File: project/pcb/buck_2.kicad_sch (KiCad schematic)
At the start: 15 parts, among them U1 IR2110PBF DIP14, U2 L7805CV, U3 SN74HCT14N

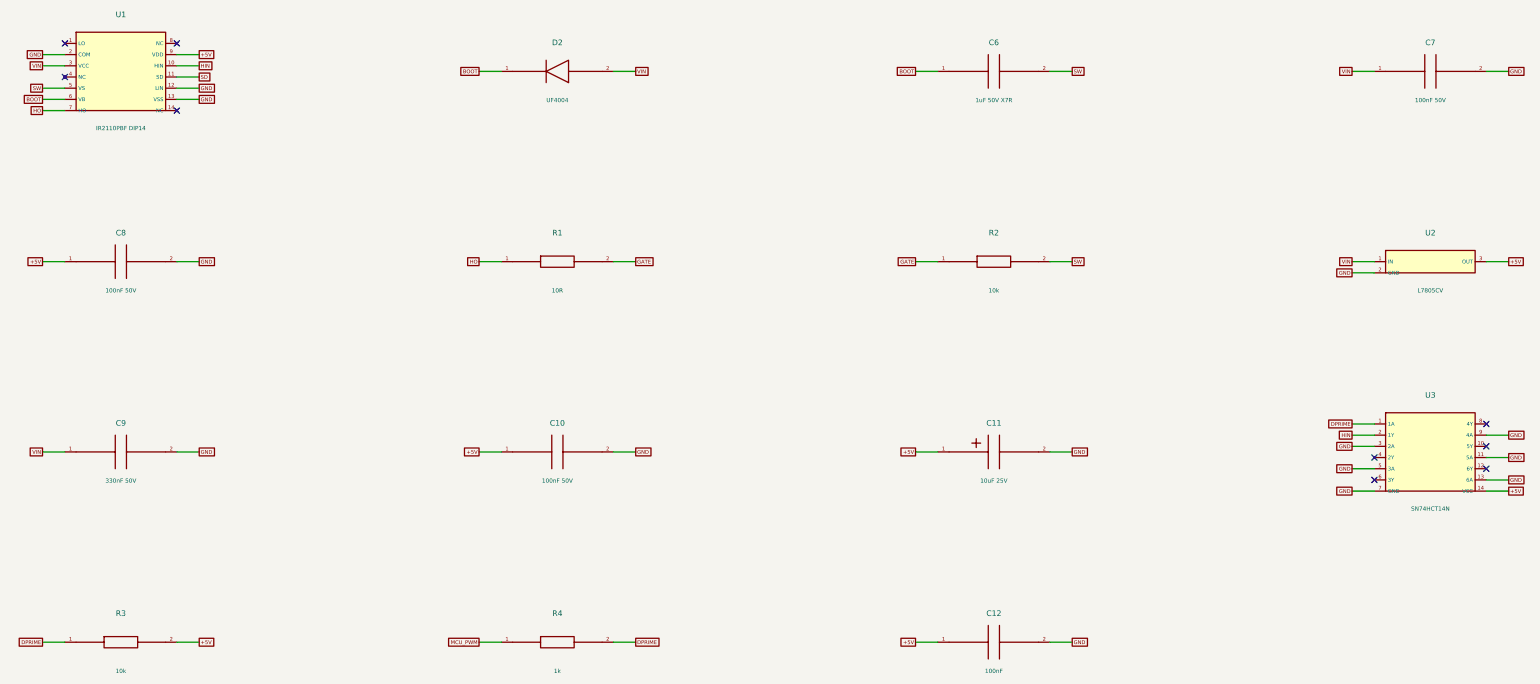
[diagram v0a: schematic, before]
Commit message: Preserve Buck PCB design and add validated JLCPCB quote package
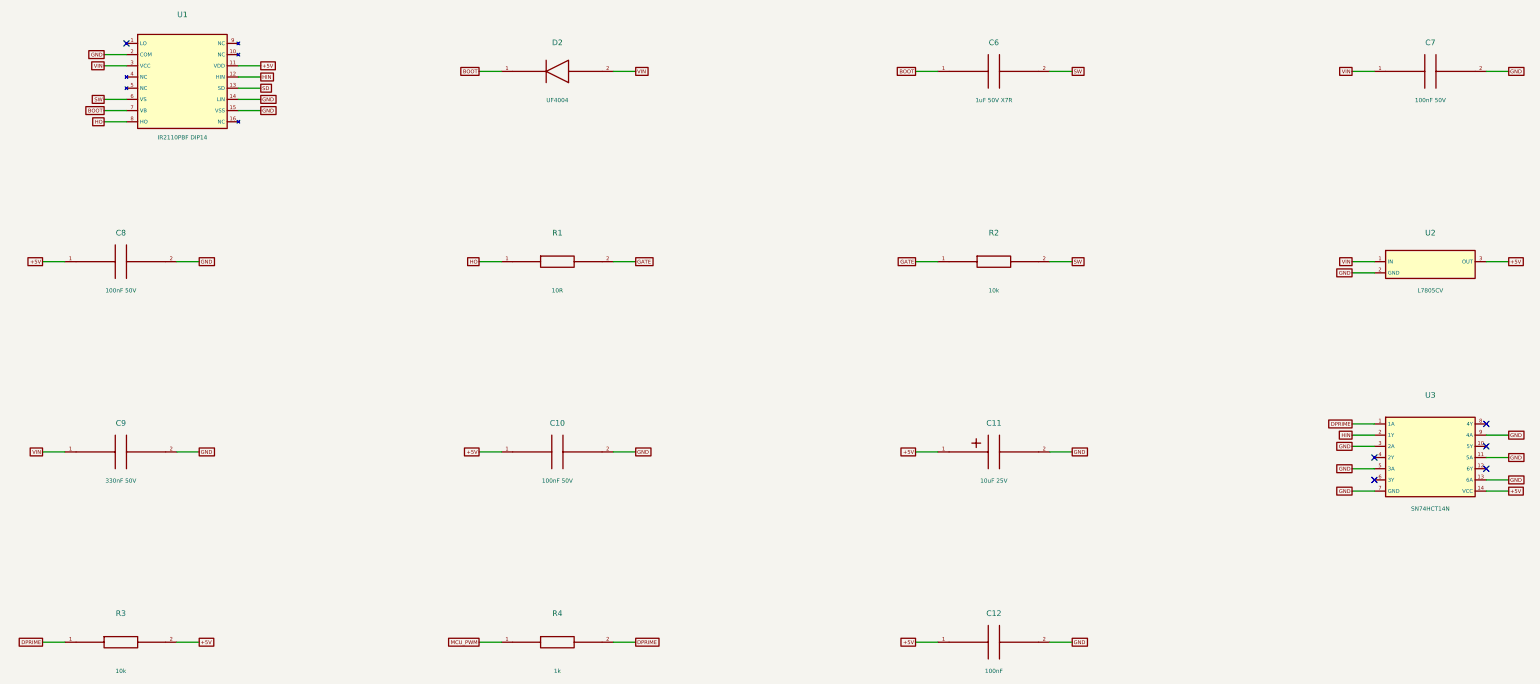
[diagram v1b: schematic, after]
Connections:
- net +5V: now also U1.11 (VDD); no longer U1.9 (VDD)
- net BOOT: now also U1.7 (VB); no longer U1.6 (VB)
- net GND: now also U1.14 (LIN), U1.15 (VSS); no longer U1.12 (LIN), U1.13 (VSS)
- net HIN: now also U1.12 (HIN); no longer U1.10 (HIN)
- net HO: now also U1.8 (HO); no longer U1.7 (HO)
- net SD: now also U1.13 (SD); no longer U1.11 (SD)
- net SW: now also U1.6 (VS); no longer U1.5 (VS)
- no-connect marks 9 -> 6
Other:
- moved on the sheet: U3
